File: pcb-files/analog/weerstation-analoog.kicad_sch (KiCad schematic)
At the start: 56 parts, among them J1 i2c in out, J10 regensensor2 pins, J11 adc_alerts, J12 sound meter, J13 ADC 4 inputs, J2 power-in, J3 ads1115 (1), J4 ads1115 (2), J5 ads1115 (4), J6 ads1115 (3)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

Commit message: update pcb files better layout and grounding inproved
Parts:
- added H1, H2, H3, H4: MountingHole_Pad, MountingHole:MountingHole_2.7mm_M2.5_Pad, symbol Mechanical:MountingHole_Pad
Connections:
- net GND: now also H1.1, H2.1, H3.1, H4.1

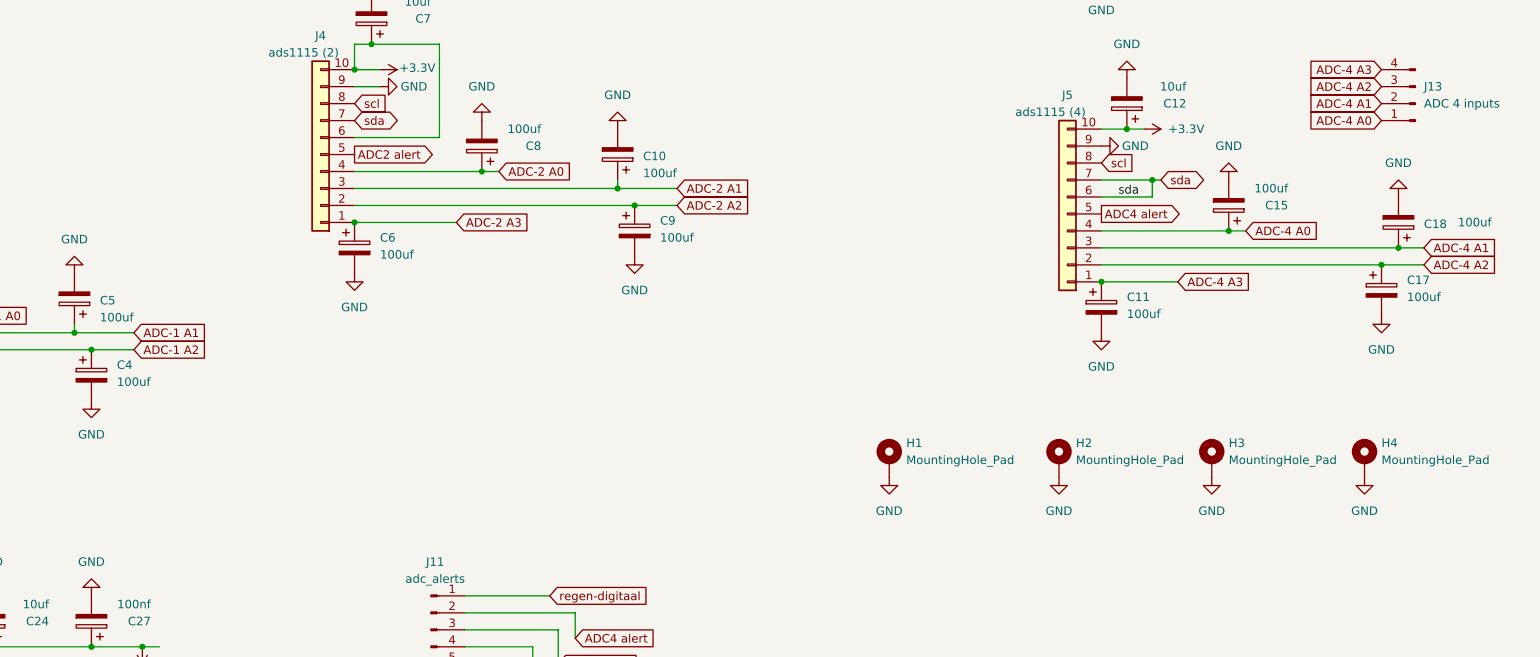
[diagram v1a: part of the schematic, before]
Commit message: pcbs as orderd. loads of grounding fixes
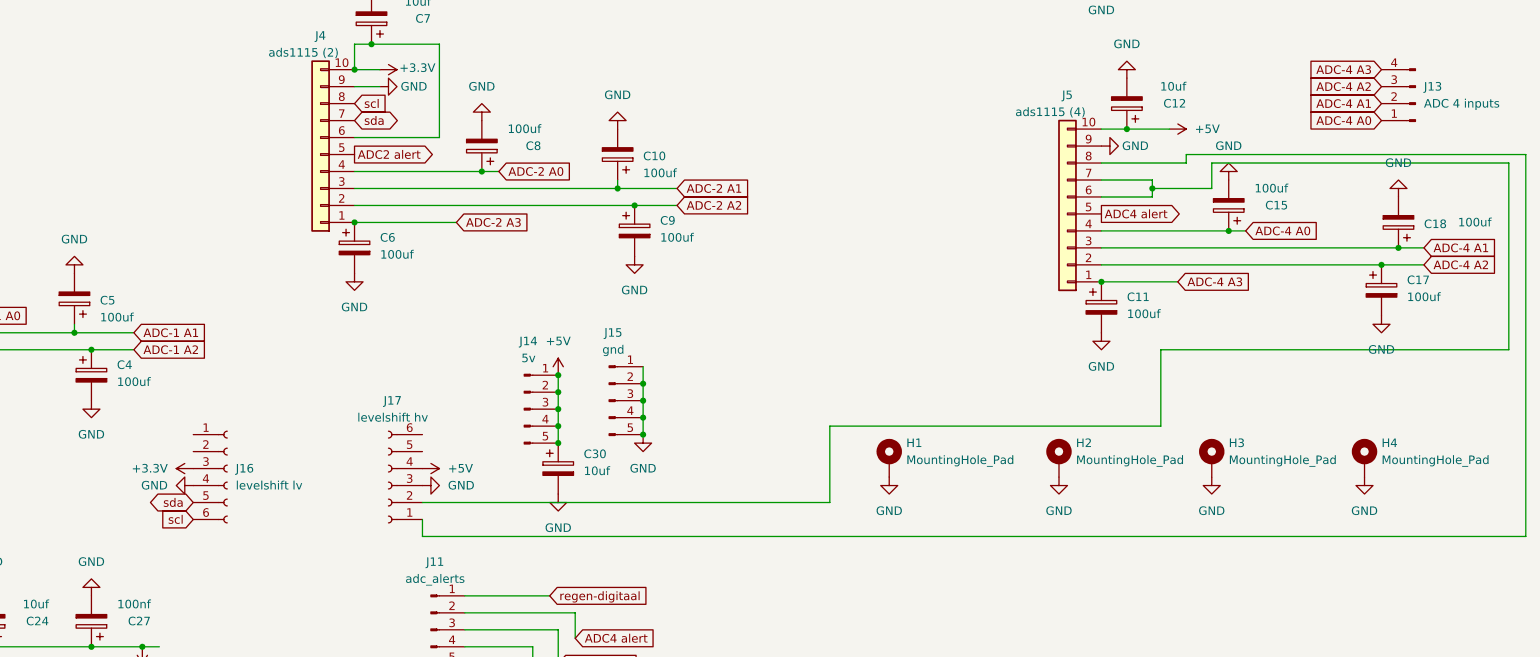
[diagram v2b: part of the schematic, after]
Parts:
- added C30: 10uf, Capacitor_SMD:C_1206_3216Metric_Pad1.33x1.80mm_HandSolder, symbol Device:C_Polarized
- added J14: 5v, Connector_PinHeader_2.54mm:PinHeader_1x05_P2.54mm_Vertical, symbol Connector:Conn_01x05_Pin
- added J15: gnd, Connector_PinHeader_2.54mm:PinHeader_1x05_P2.54mm_Vertical, symbol Connector:Conn_01x05_Pin
- added J16: levelshift lv, Connector_PinSocket_2.54mm:PinSocket_1x06_P2.54mm_Vertical, symbol Connector:Conn_01x06_Socket
- added J17: levelshift hv, Connector_PinSocket_2.54mm:PinSocket_1x06_P2.54mm_Vertical, symbol Connector:Conn_01x06_Socket
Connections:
- net +3.3V: now also J16.3 (Pin_3); no longer C12.1, J5.10 (Pin_10)
- net +5V: now also C12.1, J5.10 (Pin_10), C30.1, J14.1 (Pin_1), J14.2 (Pin_2), J14.3 (Pin_3), J14.4 (Pin_4), J14.5 (Pin_5), J17.4 (Pin_4)
- net GND: now also C30.2, J15.1 (Pin_1), J15.2 (Pin_2), J15.3 (Pin_3), J15.4 (Pin_4), J15.5 (Pin_5), J16.4 (Pin_4), J17.3 (Pin_3)
- net scl: now also J16.6 (Pin_6); no longer J5.8 (Pin_8)
- net sda: now also J16.5 (Pin_5); no longer J5.6 (Pin_6), J5.7 (Pin_7)
- new net: J17.2 (Pin_2), J5.6 (Pin_6), J5.7 (Pin_7)
- new net: J17.1 (Pin_1), J5.8 (Pin_8)
